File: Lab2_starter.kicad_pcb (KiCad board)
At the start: 4 copper layers, 187.3 x 181.2 mm, 77 parts, among them J1 973582101, J10 Conn_01x02, J11 Conn_01x02, J12 Conn_01x02, J13 Conn_01x02, J14 Conn_01x02, J15 Conn_01x02, J16 Conn_01x02, J2 973582100, J3 973582101, J4 973582100, J5 Conn_01x01, J6 Conn_01x01, J7 Conn_01x02, J8 Conn_01x02, J9 Conn_01x02, Q1 NMOS, Q2 NMOS, SW1 SW_Push_DPDT, U1 IR2010, U2 CT416-HSN820DR, U3 LAUNCHXL-F28P55X_BottomHalf

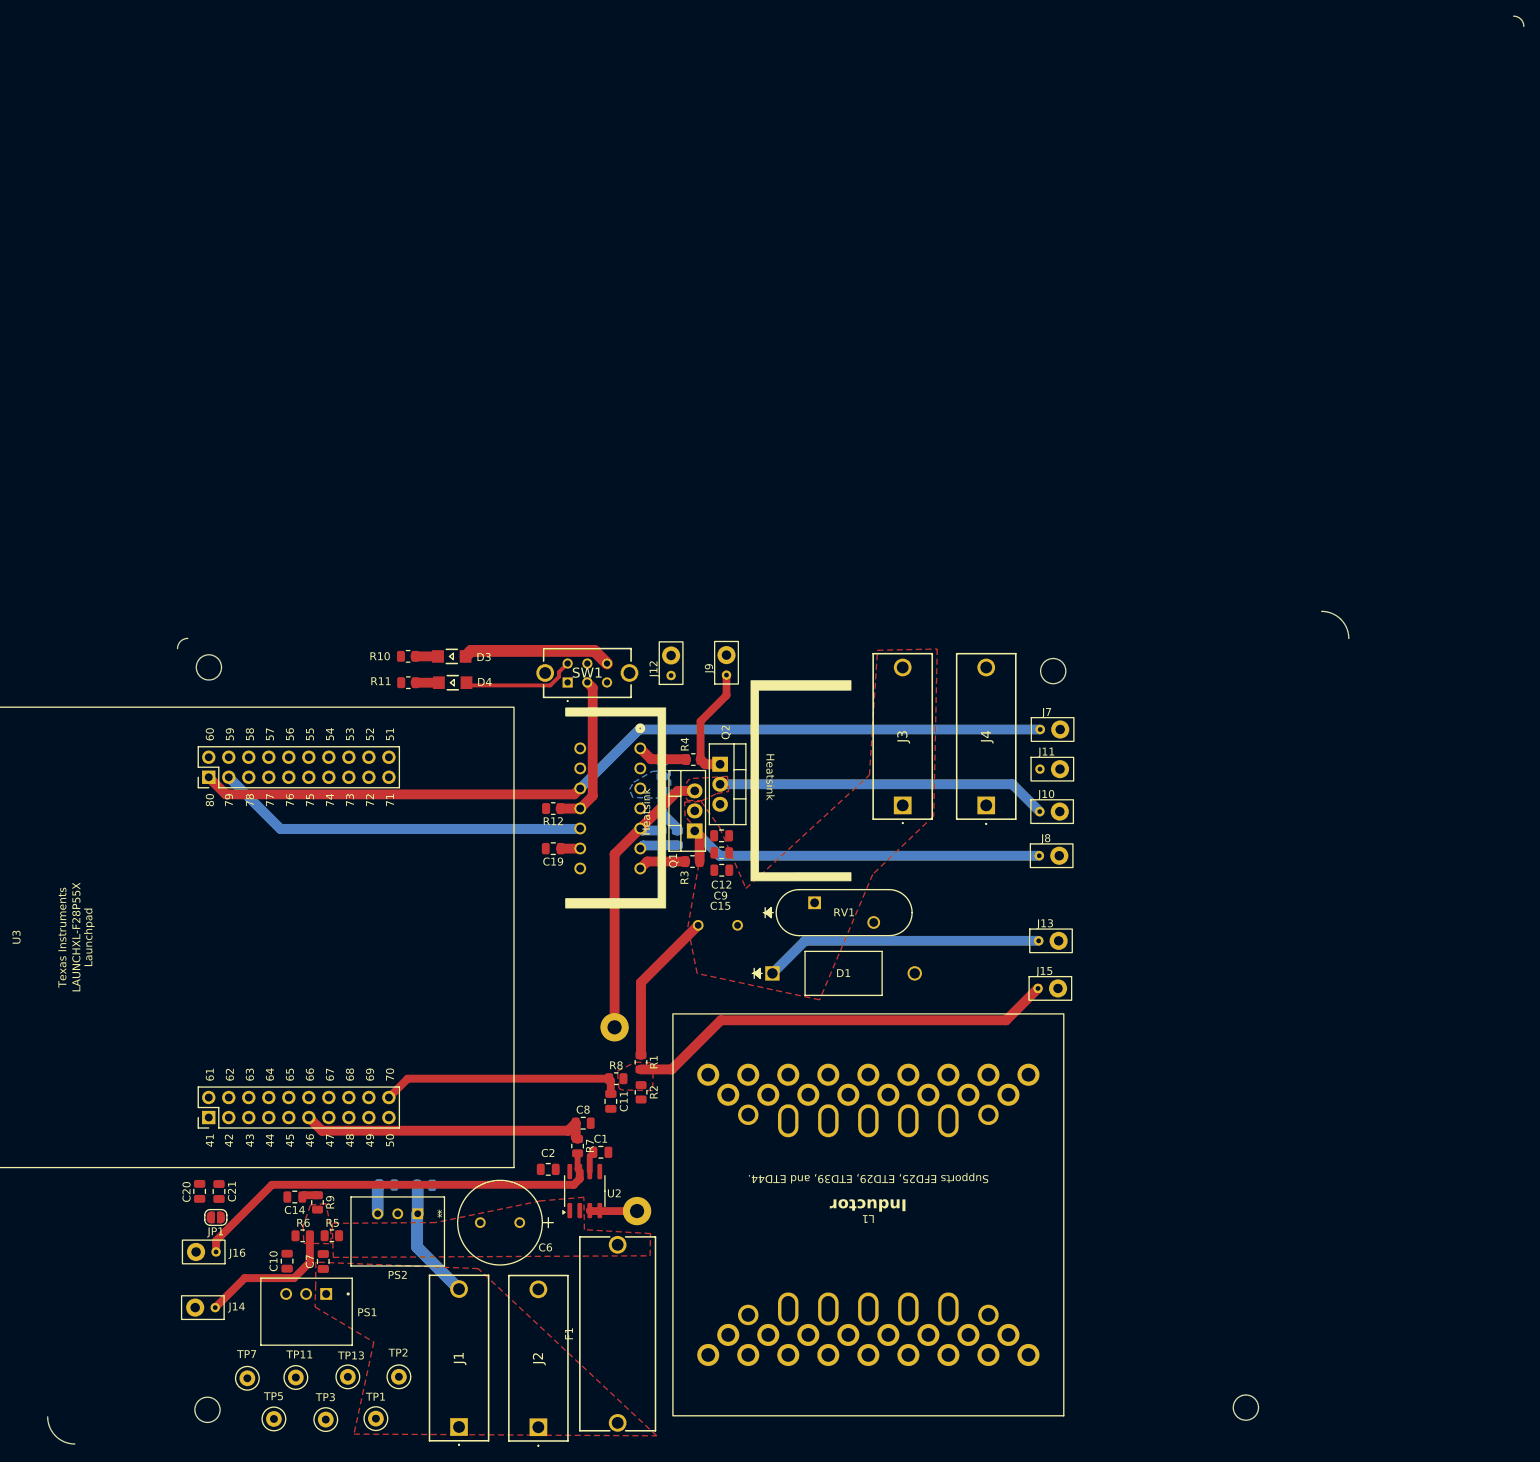
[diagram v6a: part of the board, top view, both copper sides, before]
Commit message: Edge Cuts + Test Points
Edge cuts, tucked right PCB edge in, moved test points and redid the test point routing for cleanliness
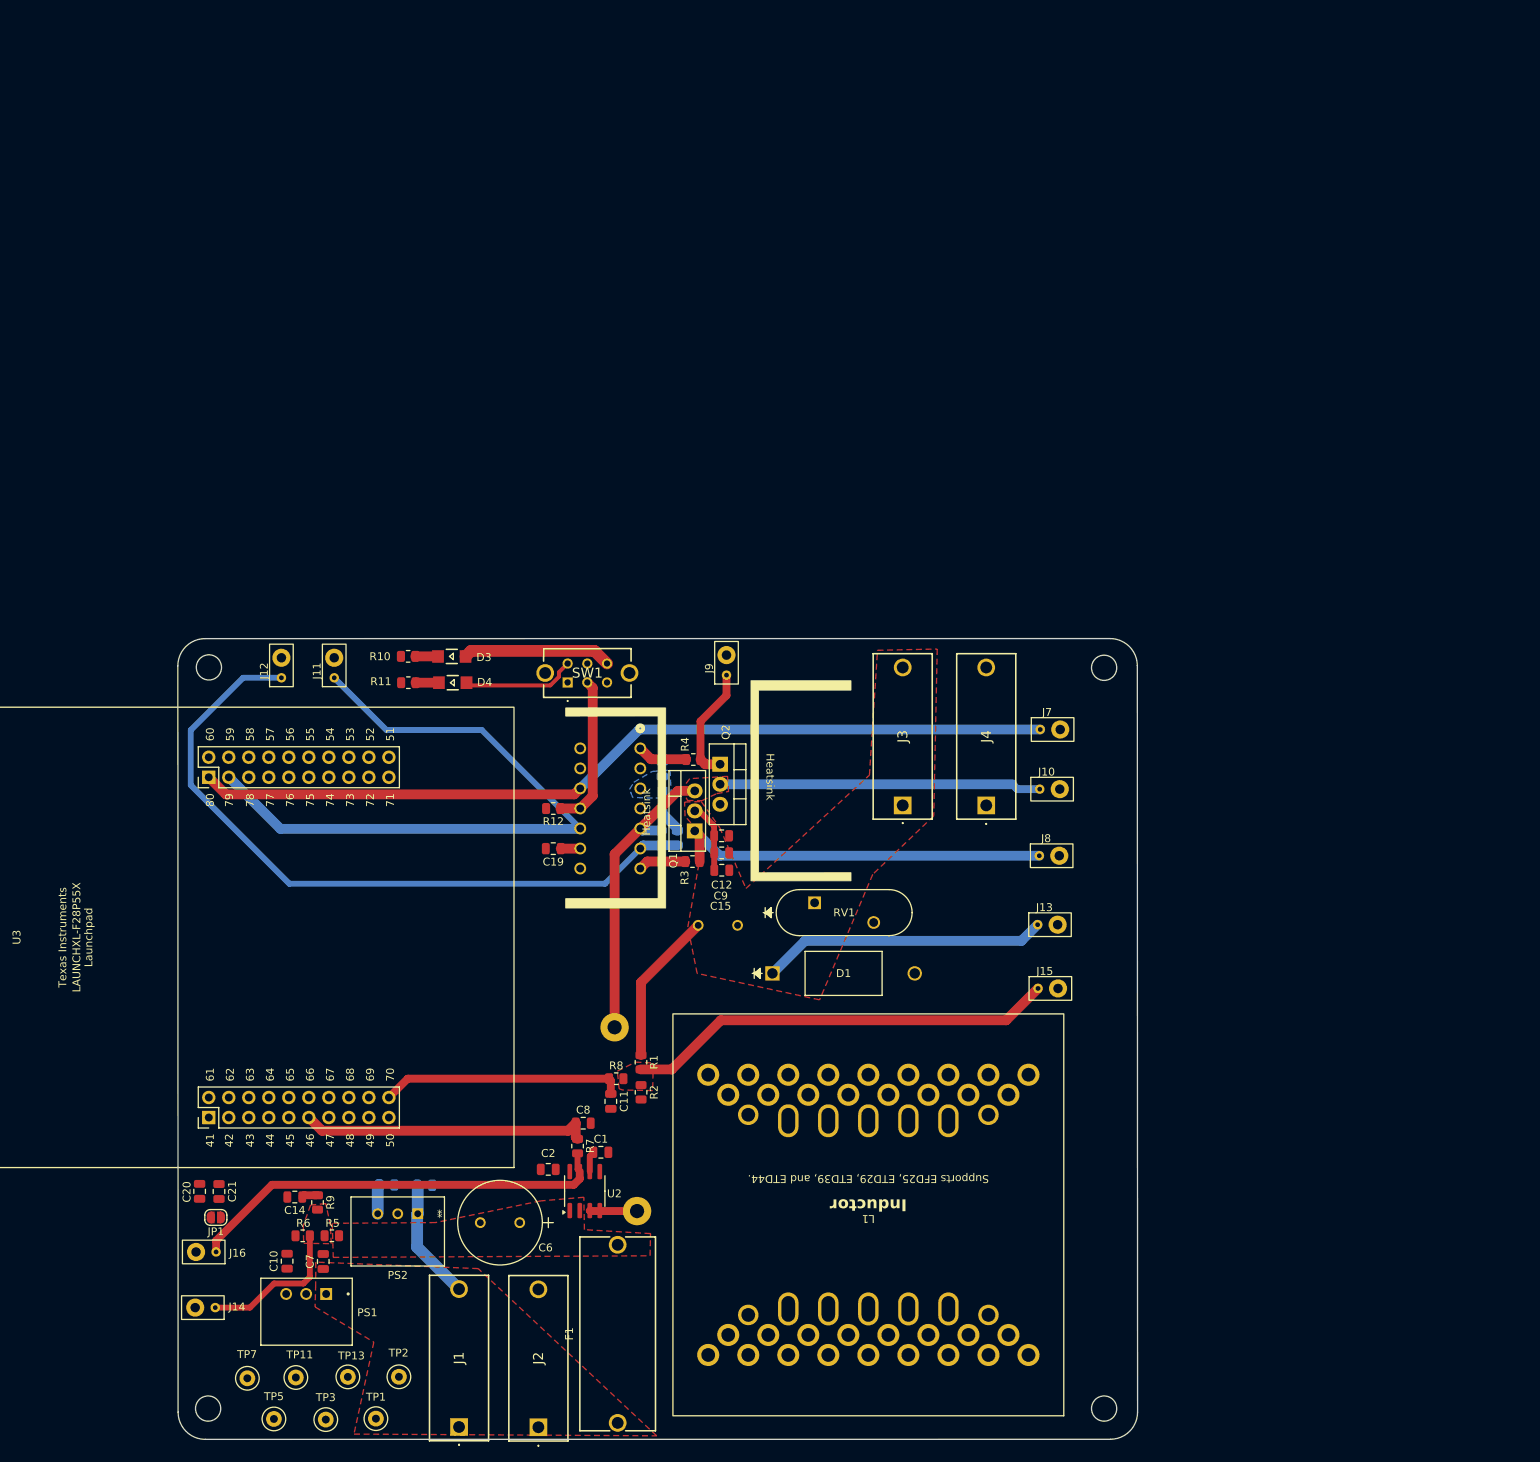
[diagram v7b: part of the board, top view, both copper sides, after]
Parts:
- moved J11 91.7 mm to (39.9, 41.6), turned to 90 degrees
- moved J12 49.5 mm to (33.2, 41.6)
- moved H3 18.0 mm to (137.6, 135.6)
- moved H1 6.47 mm to (137.6, 41.6)
- moved J10 2.85 mm to (130.7, 57.0)
- moved J13 2.05 mm to (130.4, 74.2)
- moved H2 0.18 mm to (23.9, 135.6)
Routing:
- net Vboot: track 4.88 -> 90.2 mm
- net C2000 D': track 47.3 -> 86.5 mm
- net Vout: track 55.2 -> 64.8 mm
- net Vin_sens: track 17.8 -> 19.1 mm
- net Vsw: track 80.2 -> 79.0 mm
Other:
- board size 187.3 x 181.2 mm -> 121.8 x 101.6 mm

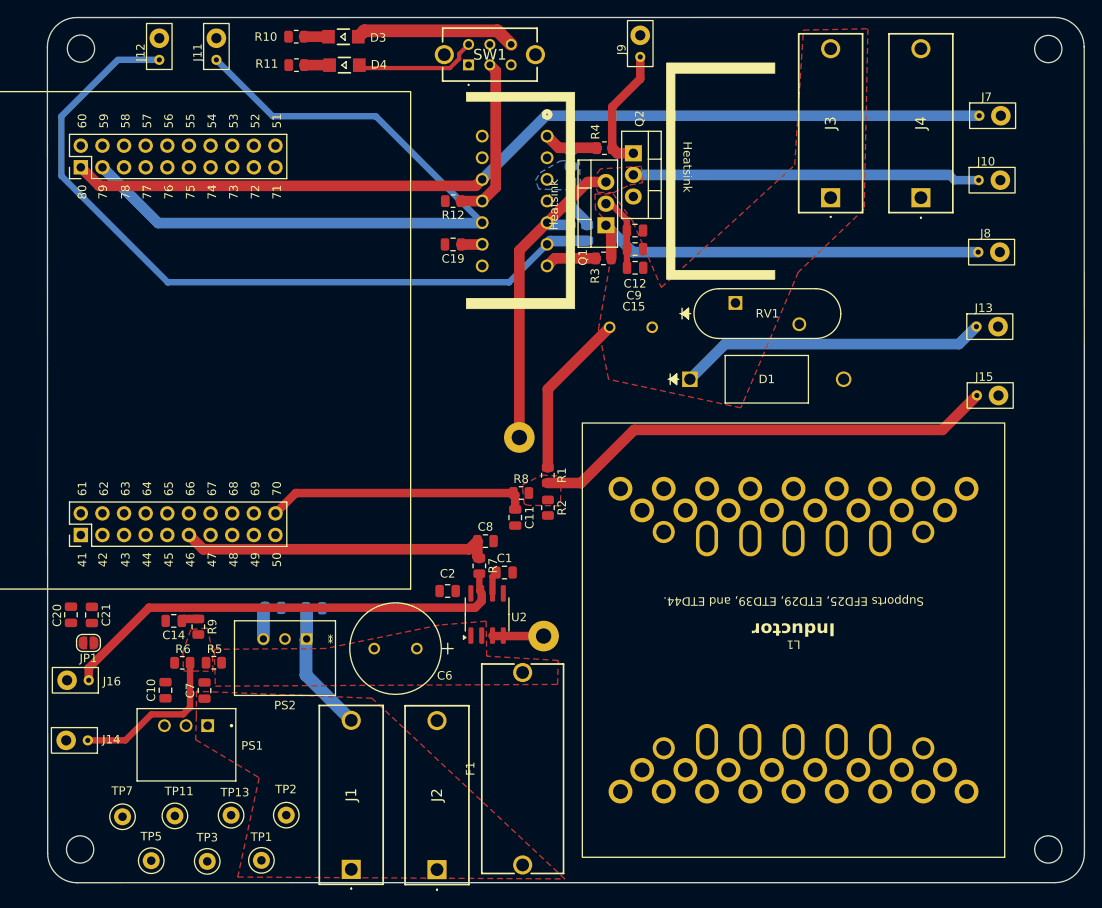
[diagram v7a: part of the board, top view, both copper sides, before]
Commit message: Added planes and fixed for DRC
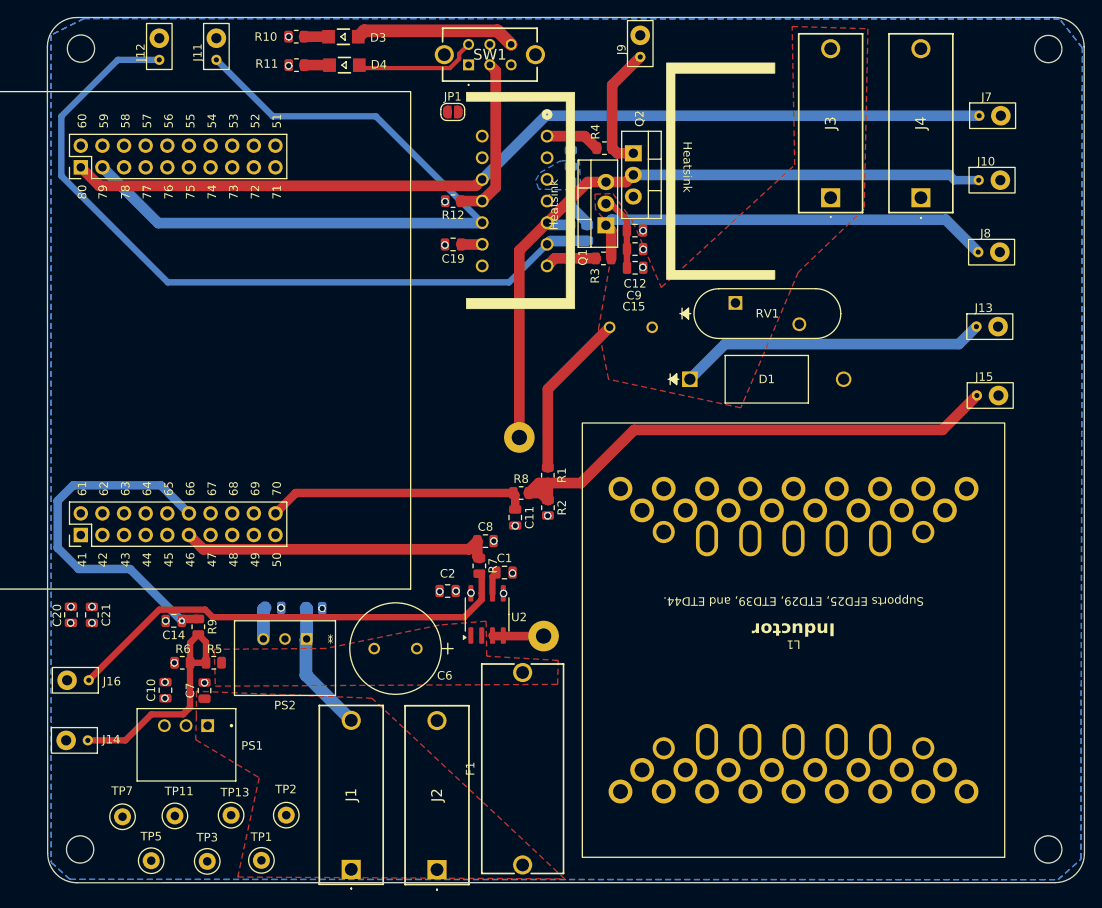
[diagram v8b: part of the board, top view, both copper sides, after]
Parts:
- moved JP1 75.6 mm to (67.7, 49.0), turned to 0 degrees
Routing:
- net /ADCINA4: track 2.03 -> 43.2 mm, vias 0 -> 1
- net Vin_sens: track 19.1 -> 28.1 mm
- net Vout_sens: track 54.6 -> 61.9 mm
- net Vsw: track 79.0 -> 82.6 mm
- net D': track 49.2 -> 49.7 mm
- net GND: vias 0 -> 21
- net +3.3V: vias 0 -> 6
- added copper zone on In2.Cu, net +3.3V
- added copper zone on In1.Cu, net GND
- added copper zone on F.Cu, net Vout
- removed copper zone on F.Cu, net (none)
- removed copper zone on F.Cu, net Vin_sens
- removed copper zone on F.Cu, net Vout_sens
- removed copper zone on F.Cu, net Vsw
